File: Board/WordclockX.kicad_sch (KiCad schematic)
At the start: 87 parts, among them J1 USB_C_Receptacle_USB2.0, SW1 SW_Push_Dual, SW2 SW_Push_Dual, U1 W25Q16JLSNIG, U2 MCP7940N-xST, U3 RP2040, U4 MIC5504-3.3YM5, U5 74HCT137, U6 PCA9626, U7 PCA9626, Y1 12M, Y2 32768

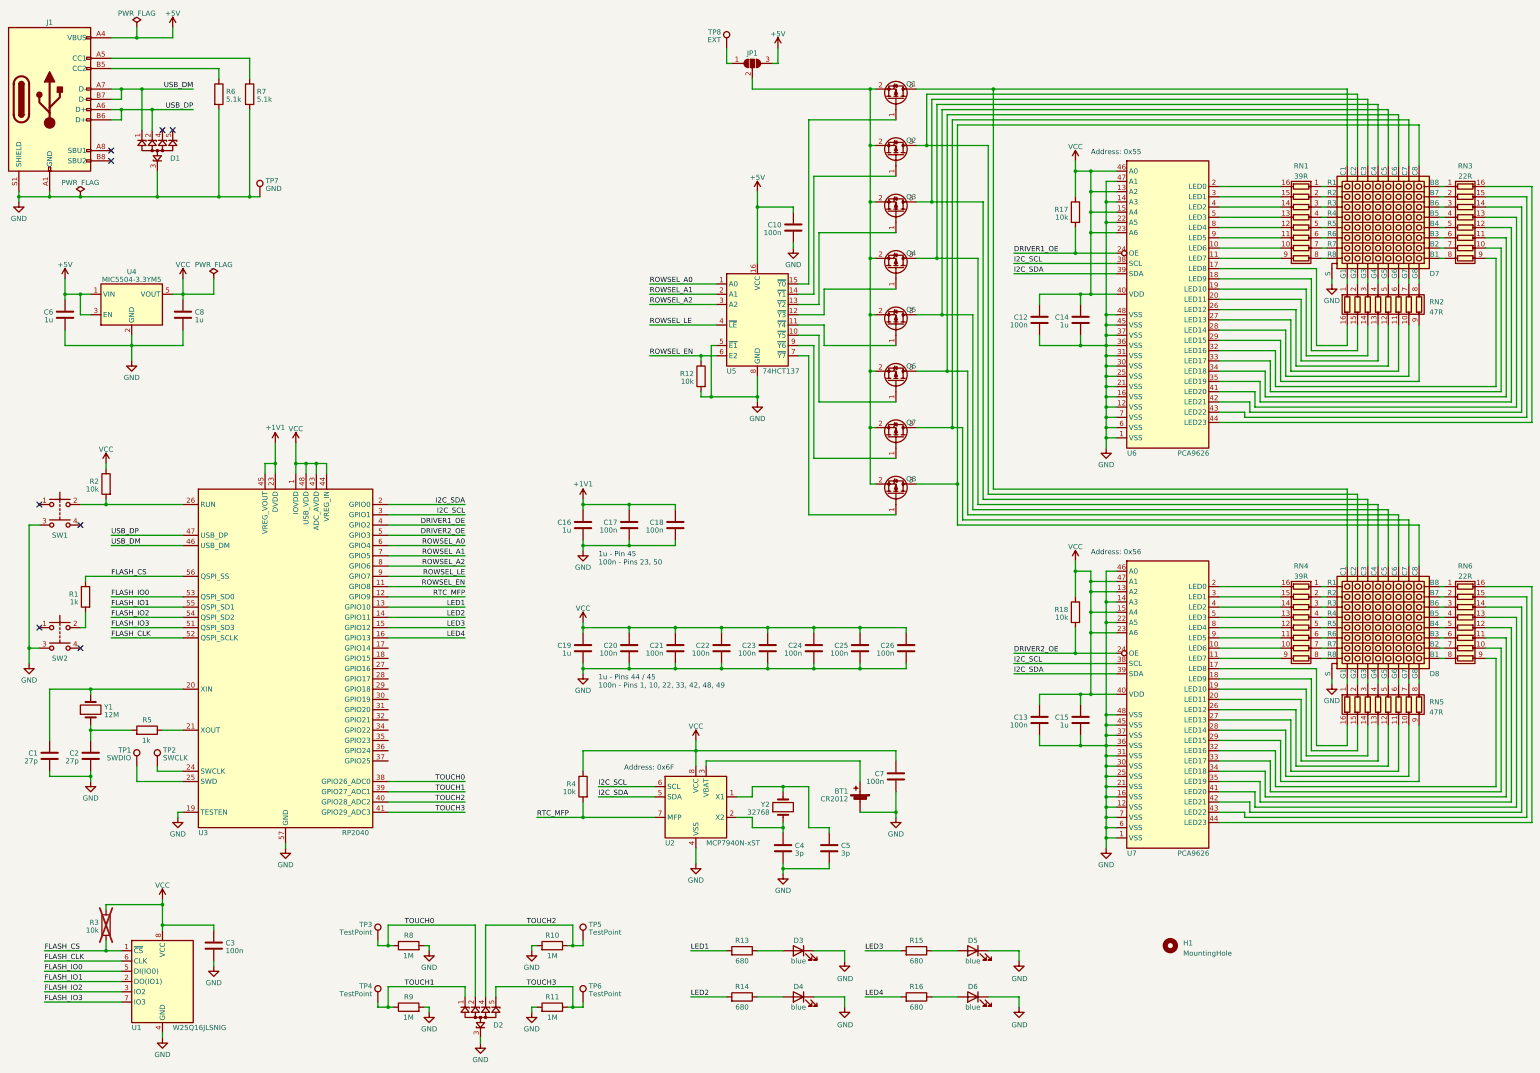
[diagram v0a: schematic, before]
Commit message: Added product links and footprints to resistor arrays
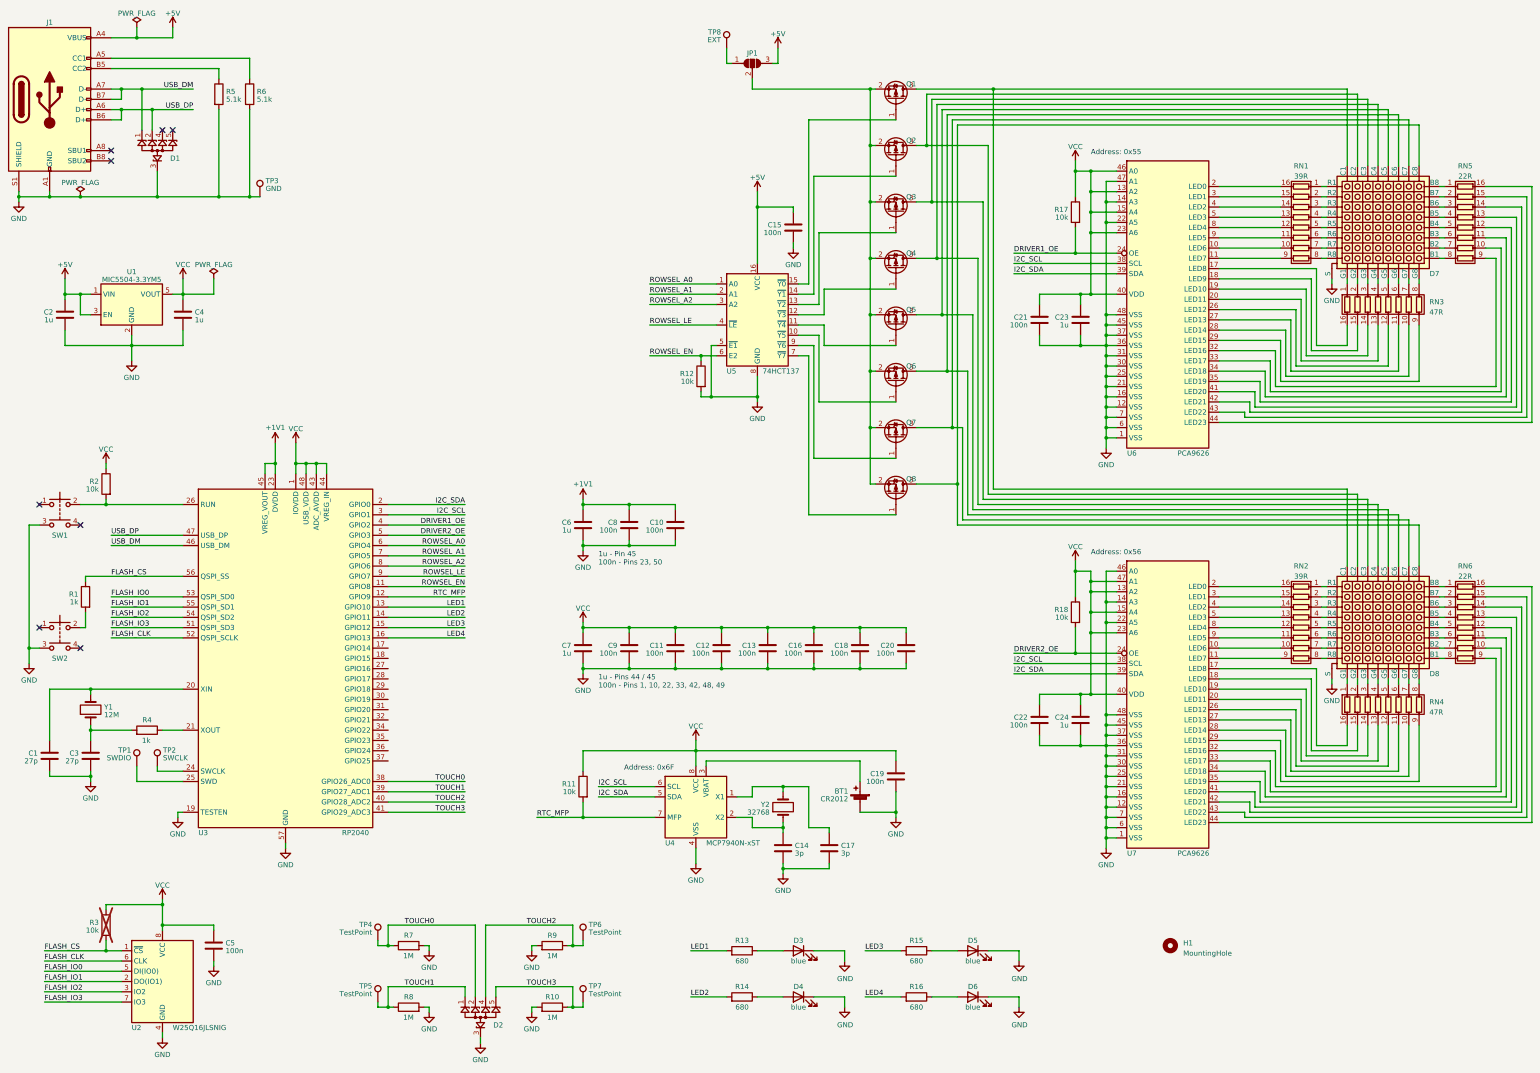
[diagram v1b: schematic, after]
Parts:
- removed RN5: 47R, symbol Device:R_Pack08
- added RN2: 39R, Resistor_SMD:R_Array_Convex_8x0602, symbol Device:R_Pack08
- RN1: footprint (none) -> Resistor_SMD:R_Array_Convex_8x0602; Mouser (none) -> 667-EXB-2HV390JV
- RN3: renamed from RN2; footprint (none) -> Resistor_SMD:R_Array_Convex_8x0602; Mouser (none) -> 667-EXB-2HV470JV
- RN4: value 39R -> 47R; footprint (none) -> Resistor_SMD:R_Array_Convex_8x0602; Mouser (none) -> 667-EXB-2HV470JV
- RN5: renamed from RN3; footprint (none) -> Resistor_SMD:R_Array_Convex_8x0602; Mouser (none) -> 667-EXB-2HV220JV
- RN6: footprint (none) -> Resistor_SMD:R_Array_Convex_8x0602; Mouser (none) -> 667-EXB-2HV220JV
- renumbered C18 to C10, C21 to C11, C22 to C12, C23 to C13, C4 to C14, C10 to C15, C24 to C16, C5 to C17, C25 to C18, C7 to C19, C6 to C2, C26 to C20, C12 to C21, C13 to C22, C14 to C23, C15 to C24, C2 to C3, C8 to C4, C3 to C5, C16 to C6, C19 to C7, C17 to C8, C20 to C9, R11 to R10, R4 to R11, R5 to R4, R6 to R5, R7 to R6, R8 to R7, R9 to R8, R10 to R9, TP7 to TP3, TP3 to TP4, TP4 to TP5, TP5 to TP6, TP6 to TP7, U4 to U1, U1 to U2, U2 to U4
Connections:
- net at U7.10 (LED6): now also RN2.10 (R7.2); no longer RN4.10 (R7.2)
- net at U7.11 (LED7): now also RN2.9 (R8.2); no longer RN4.9 (R8.2)
- net at U7.17 (LED8): now also RN4.16 (R1.2)
- net at U7.18 (LED9): now also RN4.15 (R2.2)
- net at U7.19 (LED10): now also RN4.14 (R3.2)
- net at U7.2 (LED0): now also RN2.16 (R1.2); no longer RN4.16 (R1.2)
- net at U7.20 (LED11): now also RN4.13 (R4.2)
- net at U7.26 (LED12): now also RN4.12 (R5.2)
- net at U7.27 (LED13): now also RN4.11 (R6.2)
- net at U7.28 (LED14): now also RN4.10 (R7.2)
- net at U7.29 (LED15): now also RN4.9 (R8.2)
- net at U7.3 (LED1): now also RN2.15 (R2.2); no longer RN4.15 (R2.2)
- net at U7.4 (LED2): now also RN2.14 (R3.2); no longer RN4.14 (R3.2)
- net at U7.5 (LED3): now also RN2.13 (R4.2); no longer RN4.13 (R4.2)
- net at U7.8 (LED4): now also RN2.12 (R5.2); no longer RN4.12 (R5.2)
- net at U7.9 (LED5): now also RN2.11 (R6.2); no longer RN4.11 (R6.2)
- net at D8.9 (R1): now also RN2.1 (R1.1); no longer RN4.1 (R1.1)
- net at D8.10 (R2): now also RN2.2 (R2.1); no longer RN4.2 (R2.1)
- net at D8.11 (R3): now also RN2.3 (R3.1); no longer RN4.3 (R3.1)
- net at D8.12 (R4): now also RN2.4 (R4.1); no longer RN4.4 (R4.1)
- net at D8.13 (R5): now also RN2.5 (R5.1); no longer RN4.5 (R5.1)
- net at D8.14 (R6): now also RN2.6 (R6.1); no longer RN4.6 (R6.1)
- net at D8.15 (R7): now also RN2.7 (R7.1); no longer RN4.7 (R7.1)
- net at D8.16 (R8): now also RN2.8 (R8.1); no longer RN4.8 (R8.1)
- net at D8.28 (G1): now also RN4.1 (R1.1)
- net at D8.27 (G2): now also RN4.2 (R2.1)
- net at D8.26 (G3): now also RN4.3 (R3.1)
- net at D8.25 (G4): now also RN4.4 (R4.1)
- net at D8.24 (G5): now also RN4.5 (R5.1)
- net at D8.23 (G6): now also RN4.6 (R6.1)
- net at D8.22 (G7): now also RN4.7 (R7.1)
- net at D8.21 (G8): now also RN4.8 (R8.1)

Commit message: Assigned missing footprints
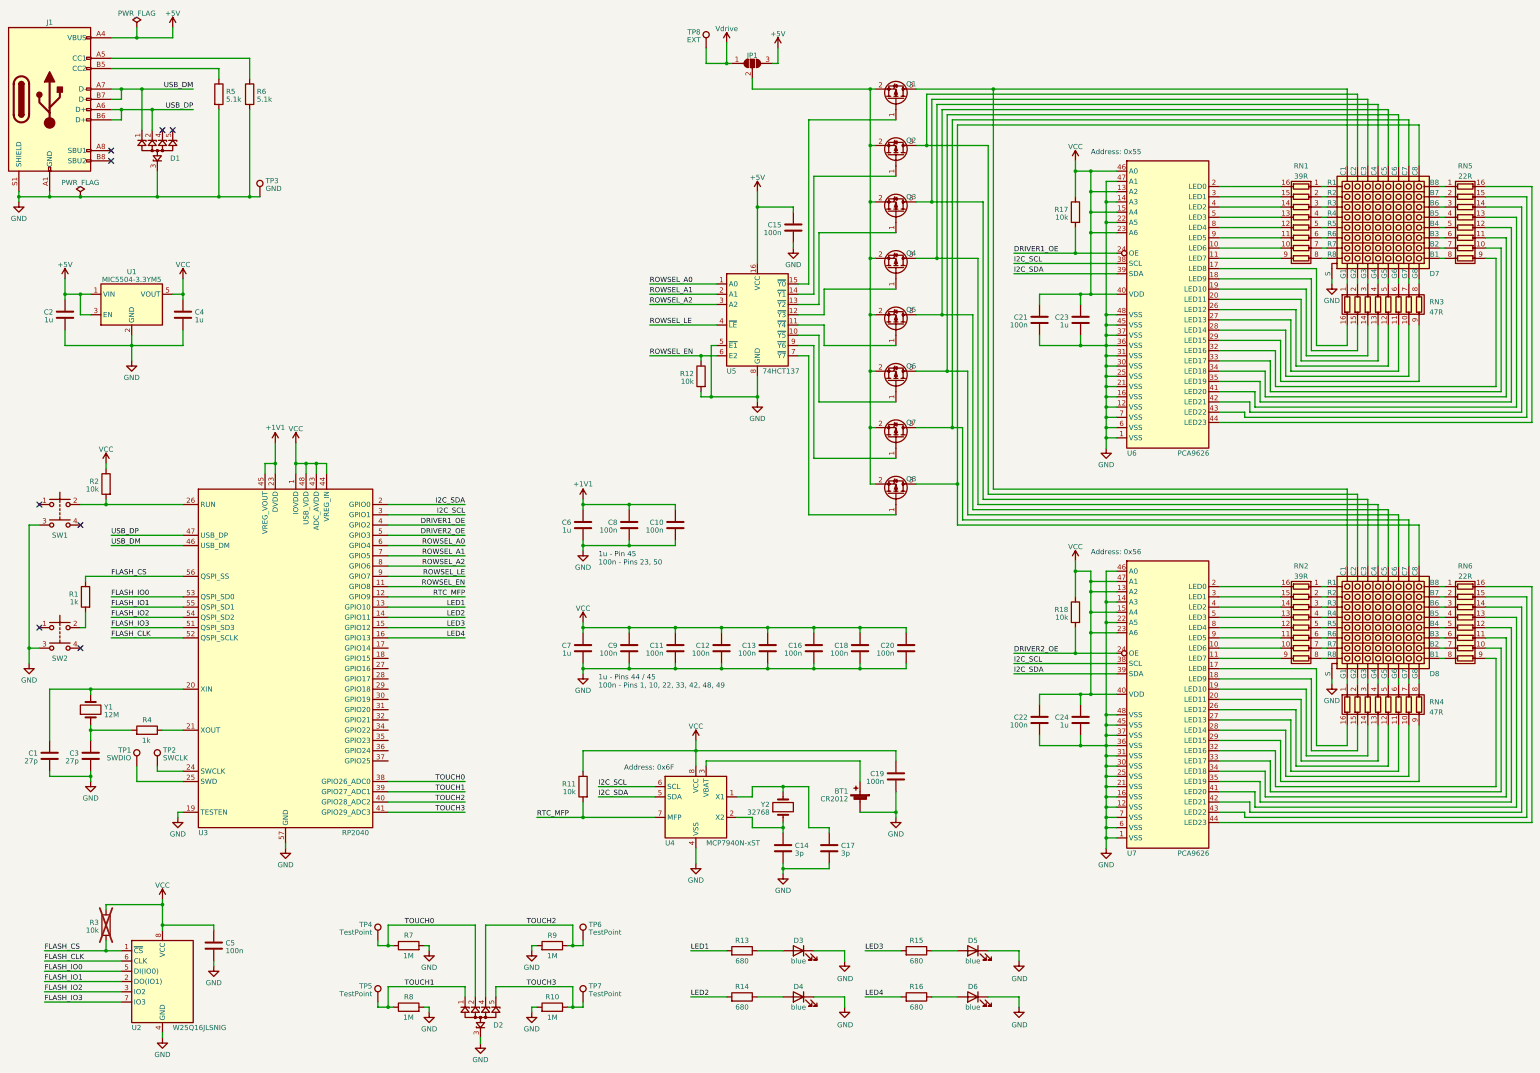
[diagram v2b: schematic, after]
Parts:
- removed H1: MountingHole, symbol Mechanical:MountingHole
- C1, C10, C11, C12, C13, C14, C15, C16, C17, C18, C19, C20, C21, C22, C3, C5, C8, C9: footprint (none) -> Capacitor_SMD:C_0603_1608Metric
- C2, C23, C24, C4, C6, C7: footprint (none) -> Capacitor_SMD:C_0805_2012Metric
- JP1: footprint (none) -> Jumper:SolderJumper-3_P1.3mm_Open_RoundedPad1.0x1.5mm
- TP1, TP2, TP3, TP8: footprint (none) -> TestPoint:TestPoint_Pad_1.0x1.0mm
- TP4, TP5, TP6, TP7: footprint (none) -> TestPoint:TestPoint_Pad_D4.0mm
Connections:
- net Vdrive: now reaches JP1.1 (A), TP8.1
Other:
- moved on the sheet: TP8

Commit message: Placement of components done
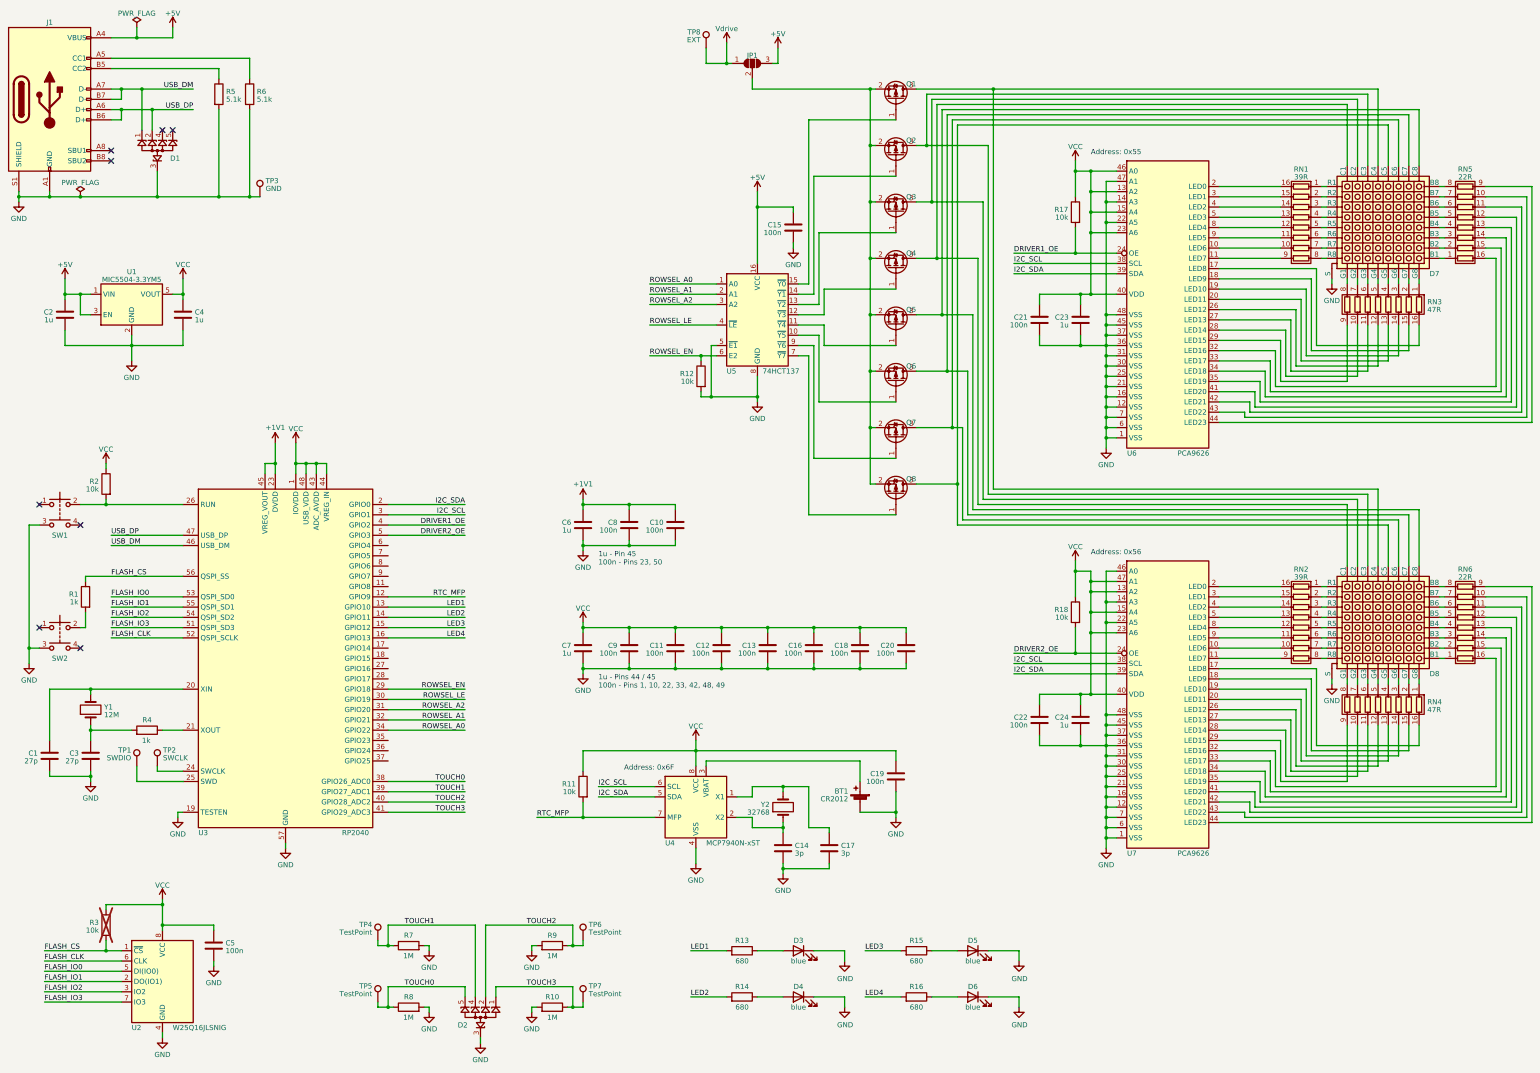
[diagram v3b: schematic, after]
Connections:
- net ROWSEL_A0: now also U3.34 (GPIO22); no longer U3.6 (GPIO4)
- net ROWSEL_A1: now also U3.32 (GPIO21); no longer U3.7 (GPIO5)
- net ROWSEL_A2: now also U3.31 (GPIO20); no longer U3.8 (GPIO6)
- net ROWSEL_EN: now also U3.29 (GPIO18); no longer U3.11 (GPIO8)
- net ROWSEL_LE: now also U3.30 (GPIO19); no longer U3.9 (GPIO7)
- net TOUCH0: now also D2.5 (Ch.4), D2.6 (Ch.4), R8.1, TP5.1; no longer D2.2 (Ch.2), R7.1, TP4.1
- net TOUCH1: now also D2.4 (Ch.3), D2.7 (Ch.3), R7.1, TP4.1; no longer D2.1 (Ch.1), R8.1, TP5.1
- net TOUCH2: now also D2.2 (Ch.2), D2.9 (Ch.2); no longer D2.4 (Ch.3)
- net TOUCH3: now also D2.1 (Ch.1), D2.10 (Ch.1); no longer D2.5 (Ch.4)
- net USB_DM: now also D1.10 (Ch.1)
- net USB_DP: now also D1.9 (Ch.2)
- net at U7.32 (LED16): now also RN6.16 (R1.2); no longer RN6.9 (R8.2)
- net at U7.33 (LED17): now also RN6.15 (R2.2); no longer RN6.10 (R7.2)
- net at U7.34 (LED18): now also RN6.14 (R3.2); no longer RN6.11 (R6.2)
- net at U7.35 (LED19): now also RN6.13 (R4.2); no longer RN6.12 (R5.2)
- net at U7.41 (LED20): now also RN6.12 (R5.2); no longer RN6.13 (R4.2)
- net at U7.42 (LED21): now also RN6.11 (R6.2); no longer RN6.14 (R3.2)
- net at U7.43 (LED22): now also RN6.10 (R7.2); no longer RN6.15 (R2.2)
- net at U7.44 (LED23): now also RN6.9 (R8.2); no longer RN6.16 (R1.2)
- net at D7.29 (C5), D8.29 (C5): now also Q8.3 (D); no longer Q5.3 (D)
- net at D1.4 (Ch.3): now also D1.7 (Ch.3)
- net at D1.5 (Ch.4): now also D1.6 (Ch.4)
- net at D7.18 (C2), D8.18 (C2): now also Q3.3 (D); no longer Q2.3 (D)
- net at D7.17 (C1), D8.17 (C1): now also Q4.3 (D); no longer Q1.3 (D)
- net at D7.1 (B1): now also RN5.1 (R1.1); no longer RN5.8 (R8.1)
- net at D7.19 (C3), D8.19 (C3): now also Q2.3 (D); no longer Q3.3 (D)
- net at D7.2 (B2): now also RN5.2 (R2.1); no longer RN5.7 (R7.1)
- net at D7.20 (C4), D8.20 (C4): now also Q1.3 (D); no longer Q4.3 (D)
- net at D7.21 (G8): now also RN3.1 (R1.1); no longer RN3.8 (R8.1)
- net at D7.22 (G7): now also RN3.2 (R2.1); no longer RN3.7 (R7.1)
- net at D7.23 (G6): now also RN3.3 (R3.1); no longer RN3.6 (R6.1)
- net at D7.24 (G5): now also RN3.4 (R4.1); no longer RN3.5 (R5.1)
- net at D7.25 (G4): now also RN3.5 (R5.1); no longer RN3.4 (R4.1)
- net at D7.26 (G3): now also RN3.6 (R6.1); no longer RN3.3 (R3.1)
- net at D7.27 (G2): now also RN3.7 (R7.1); no longer RN3.2 (R2.1)
- net at D7.28 (G1): now also RN3.8 (R8.1); no longer RN3.1 (R1.1)
- net at D7.3 (B3): now also RN5.3 (R3.1); no longer RN5.6 (R6.1)
- net at D7.30 (C6), D8.30 (C6): now also Q7.3 (D); no longer Q6.3 (D)
- net at D7.31 (C7), D8.31 (C7): now also Q6.3 (D); no longer Q7.3 (D)
- net at D7.32 (C8), D8.32 (C8): now also Q5.3 (D); no longer Q8.3 (D)
- net at D7.4 (B4): now also RN5.4 (R4.1); no longer RN5.5 (R5.1)
- net at D7.5 (B5): now also RN5.5 (R5.1); no longer RN5.4 (R4.1)
- net at D7.6 (B6): now also RN5.6 (R6.1); no longer RN5.3 (R3.1)
- net at D7.7 (B7): now also RN5.7 (R7.1); no longer RN5.2 (R2.1)
- net at D7.8 (B8): now also RN5.8 (R8.1); no longer RN5.1 (R1.1)
- net at RN5.10 (R7.2): now also U6.43 (LED22); no longer U6.33 (LED17)
- net at RN5.11 (R6.2): now also U6.42 (LED21); no longer U6.34 (LED18)
- net at RN5.12 (R5.2): now also U6.41 (LED20); no longer U6.35 (LED19)
- net at RN5.13 (R4.2): now also U6.35 (LED19); no longer U6.41 (LED20)
- net at RN5.14 (R3.2): now also U6.34 (LED18); no longer U6.42 (LED21)
- net at RN5.15 (R2.2): now also U6.33 (LED17); no longer U6.43 (LED22)
- net at RN5.16 (R1.2): now also U6.32 (LED16); no longer U6.44 (LED23)
- net at RN5.9 (R8.2): now also U6.44 (LED23); no longer U6.32 (LED16)
- net at RN4.1 (R1.1): now also D8.21 (G8); no longer D8.28 (G1)
- net at RN4.2 (R2.1): now also D8.22 (G7); no longer D8.27 (G2)
- net at RN4.3 (R3.1): now also D8.23 (G6); no longer D8.26 (G3)
- net at RN4.4 (R4.1): now also D8.24 (G5); no longer D8.25 (G4)
- net at RN4.5 (R5.1): now also D8.25 (G4); no longer D8.24 (G5)
- net at RN4.6 (R6.1): now also D8.26 (G3); no longer D8.23 (G6)
- net at RN4.7 (R7.1): now also D8.27 (G2); no longer D8.22 (G7)
- net at RN4.8 (R8.1): now also D8.28 (G1); no longer D8.21 (G8)
- net at D8.1 (B1): now also RN6.1 (R1.1); no longer RN6.8 (R8.1)
- net at D8.2 (B2): now also RN6.2 (R2.1); no longer RN6.7 (R7.1)
- net at D8.3 (B3): now also RN6.3 (R3.1); no longer RN6.6 (R6.1)
- net at D8.4 (B4): now also RN6.4 (R4.1); no longer RN6.5 (R5.1)
- net at D8.5 (B5): now also RN6.5 (R5.1); no longer RN6.4 (R4.1)
- net at D8.6 (B6): now also RN6.6 (R6.1); no longer RN6.3 (R3.1)
- net at D8.7 (B7): now also RN6.7 (R7.1); no longer RN6.2 (R2.1)
- net at D8.8 (B8): now also RN6.8 (R8.1); no longer RN6.1 (R1.1)
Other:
- moved on the sheet: RN3, RN4
